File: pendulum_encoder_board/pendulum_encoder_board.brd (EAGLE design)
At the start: 16 x 16 mm, 4 parts

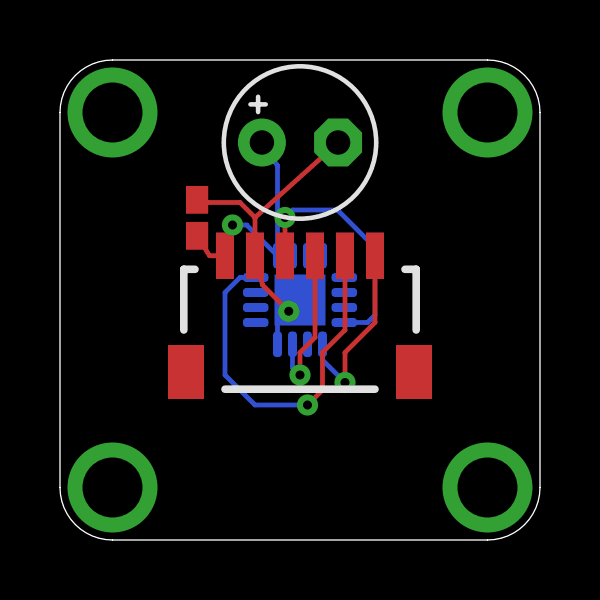
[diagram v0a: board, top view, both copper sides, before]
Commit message: fixing controller BOM mistake
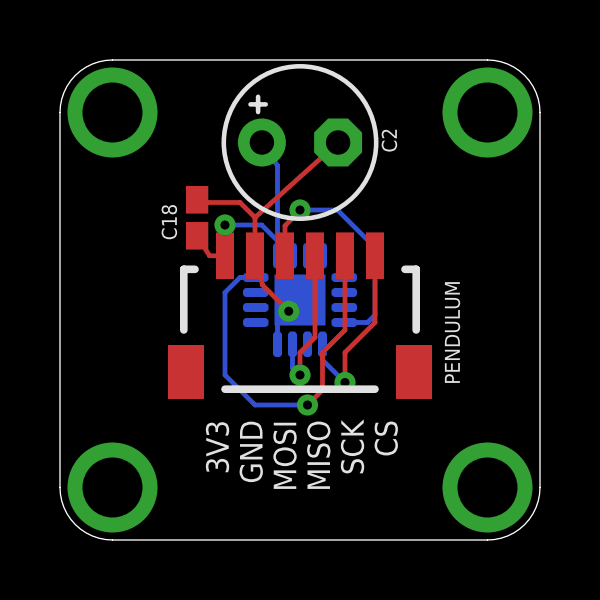
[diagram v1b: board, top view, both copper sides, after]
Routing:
- net 3V3: track 8.21 -> 8.73 mm
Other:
- board text added: "3V3 GND MOSI MISO SCK CS"
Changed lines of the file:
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@@
 <?xml version="1.0" encoding="utf-8"?>
 <!DOCTYPE eagle SYSTEM "eagle.dtd">
-<eagle version="6.5.0">
+<eagle version="9.6.2">
 <drawing>
 <settings>
 <setting alwaysvectorfont="no"/>
+<setting keepoldvectorfont="yes"/>
 <setting verticaltext="up"/>
 </settings>
@@
 <layer number="59" name="tCarbon" color="7" fill="1" visible="no" active="no"/>
 <layer number="60" name="bCarbon" color="7" fill="1" visible="no" active="no"/>
-<layer number="90" name="Modules" color="5" fill="1" visible="yes" active="yes"/>
+<layer number="90" name="Modules" color="5" fill="1" visible="no" active="no"/>
 <layer number="91" name="Nets" color="2" fill="1" visible="no" active="no"/>
 <layer number="92" name="Busses" color="1" fill="1" visible="no" active="no"/>
@@
 <wire x1="8" y1="-6.25" x2="6.25" y2="-8" width="0" layer="20" curve="-90"/>
 <wire x1="6.25" y1="8" x2="8" y2="6.25" width="0" layer="20" curve="-90"/>
+<text x="3.25" y="-4" size="0.75" layer="25" font="vector" rot="R90" align="bottom-right">3V3
+GND
+MOSI
+MISO
+SCK
+CS</text>
 </plain>
 <attributes>
@@
 <param name="dpMaxLengthDifference" value="10mm"/>
 <param name="dpGapFactor" value="2.5"/>
-<param name="checkGrid" value="0"/>
 <param name="checkAngle" value="0"/>
 <param name="checkFont" value="1"/>
 <param name="checkRestrict" value="1"/>
+<param name="checkStop" value="0"/>
+<param name="checkValues" value="0"/>
+<param name="checkNames" value="1"/>
+<param name="checkWireStubs" value="1"/>
+<param name="checkPolygonWidth" value="0"/>
 <param name="useDiameter" value="13"/>
 <param name="maxErrors" value="50"/>
@@
 <pass name="Default">
 <param name="RoutingGrid" value="50mil"/>
+<param name="AutoGrid" value="1"/>
+<param name="Efforts" value="0"/>
+<param name="TopRouterVariant" value="1"/>
 <param name="tpViaShape" value="round"/>
 <param name="PrefDir.1" value="|"/>
@@
 </autorouter>
 <elements>
-<element name="C18" library="rcl" package="C0402K" value=".1 uF" x="-3.43" y="2.74" smashed="yes" rot="R90"/>
-<element name="U$11" library="BenLibrary" package="QFN16" value="MA700" x="0" y="0" smashed="yes" rot="MR0"/>
+<element name="C18" library="rcl" package="C0402K" value=".1 uF" x="-3.43" y="2.74" smashed="yes" rot="R90">
+<attribute name="NAME" x="-4.105" y="1.99" size="0.5" layer="25" font="vector" rot="R90"/>
+</element>
+<element name="U$11" library="BenLibrary" package="QFN16" value="MA700" x="0" y="0" smashed="yes" rot="MR0">
+<attribute name="NAME" x="-2.75" y="-1.25" size="0.5" layer="26" font="vector" rot="MR90"/>
+</element>
 <element name="C2" library="rcl" package="E2,5-5" value="" x="0" y="5.25" smashed="yes">
+<attribute name="NAME" x="3.23" y="4.913" size="0.5" layer="25" font="vector" ratio="10" rot="R90"/>
 <attribute name="VALUE" x="2.413" y="2.837" size="1.27" layer="27" ratio="10"/>
 </element>
-<element name="PENDULUM" library="con-jst2" package="SM06B-SRSS-TB" value="SM06B-SRSS-TB" x="0" y="-1.5" smashed="yes"/>
+<element name="PENDULUM" library="con-jst2" package="SM06B-SRSS-TB" value="SM06B-SRSS-TB" x="0" y="-1.5" smashed="yes">
+<attribute name="NAME" x="4.83" y="0.655" size="0.5" layer="25" font="vector" rot="R270"/>
+</element>
 </elements>
 <signals>
@@
 <wire x1="-2.5" y1="1.475" x2="-3.015" y2="1.475" width="0.16" layer="1"/>
 <wire x1="-3.015" y1="1.475" x2="-3.43" y2="2.14" width="0.16" layer="1"/>
-<wire x1="-2.5" y1="1.475" x2="-2.25" y2="2.5" width="0.16" layer="1"/>
-<via x="-2.25" y="2.5" extent="1-16" drill="0.3"/>
-<wire x1="-2.25" y1="2.5" x2="-1.775" y2="2.5" width="0.16" layer="16"/>
-<wire x1="-1.775" y1="2.5" x2="-0.75" y2="1.475" width="0.16" layer="16"/>
+<wire x1="-2.5" y1="1.475" x2="-2.5" y2="2.5" width="0.16" layer="1"/>
+<via x="-2.5" y="2.5" extent="1-16" drill="0.3"/>
+<wire x1="-2.5" y1="2.5" x2="-1.275" y2="2.5" width="0.16" layer="16"/>
+<wire x1="-0.75" y1="1.975" x2="-1.275" y2="2.5" width="0.16" layer="16"/>
+<wire x1="-0.75" y1="1.975" x2="-0.75" y2="1.475" width="0.16" layer="16"/>
 </signal>
 <signal name="CS">
@@
 <wire x1="2.5" y1="-0.5" x2="2.5" y2="1.75" width="0.16" layer="16"/>
 <wire x1="2.5" y1="1.75" x2="1.25" y2="3" width="0.16" layer="16"/>
-<wire x1="1.25" y1="3" x2="-0.25" y2="3" width="0.16" layer="16"/>
-<wire x1="-0.25" y1="3" x2="-0.5" y2="2.75" width="0.16" layer="16"/>
-<via x="-0.5" y="2.75" extent="1-16" drill="0.3"/>
-<wire x1="-0.5" y1="2.75" x2="-0.5" y2="1.475" width="0.16" layer="1"/>
+<wire x1="1.25" y1="3" x2="0" y2="3" width="0.16" layer="16"/>
+<via x="0" y="3" extent="1-16" drill="0.3"/>
+<wire x1="0" y1="3" x2="0" y2="2.975" width="0.16" layer="1"/>
+<wire x1="0" y1="2.975" x2="-0.5" y2="2.475" width="0.16" layer="1"/>
+<wire x1="-0.5" y1="2.475" x2="-0.5" y2="1.475" width="0.16" layer="1"/>
 </signal>
 <signal name="MISO">
@@
 </signal>
 </signals>
+<mfgpreviewcolors>
+<mfgpreviewcolor name="soldermaskcolor" color="0xC8008000"/>
+<mfgpreviewcolor name="silkscreencolor" color="0xFFFEFEFE"/>
+<mfgpreviewcolor name="backgroundcolor" color="0xFF282828"/>
+<mfgpreviewcolor name="coppercolor" color="0xFFFFBF00"/>
+<mfgpreviewcolor name="substratecolor" color="0xFF786E46"/>
+</mfgpreviewcolors>
 </board>
 </drawing>
+<compatibility>
+<note version="6.3" minversion="6.2.2" severity="warning">
+Since Version 6.2.2 text objects can contain more than one line,
+which will not be processed correctly with this version.
+</note>
+</compatibility>
 </eagle>
